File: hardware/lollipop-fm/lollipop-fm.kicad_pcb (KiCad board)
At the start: 2 copper layers, 59 parts, among them J1 battery pads, J2 SWD, J3 USART, Q1 BC817-40W-7, Q2 BC817-40W-7, Q3 SSM3J338R, SW1 MJTP1230F, U1 STM32C011F_4-6_Px, U2 TPS61221DCK, U3 TLV9101IDCKR, U4 TLV9101IDCKR, Y1 ATS08A-E

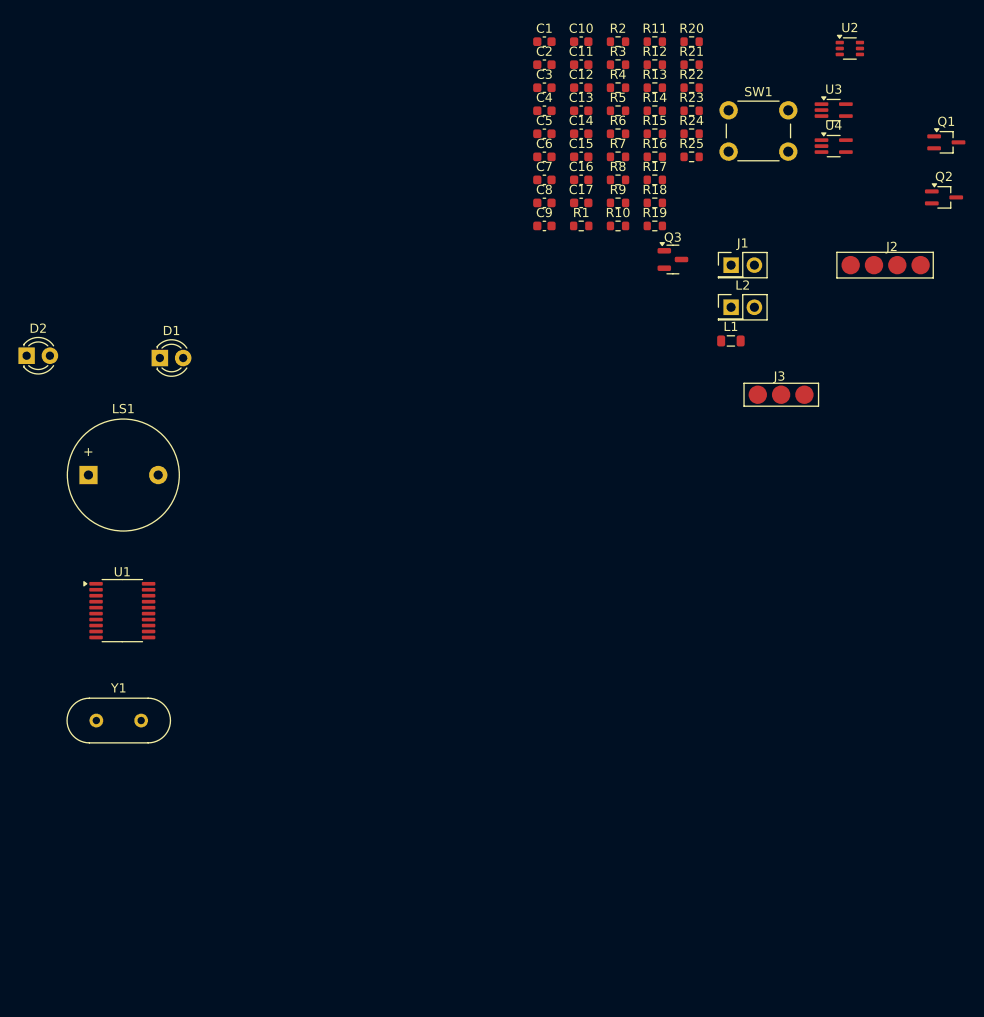
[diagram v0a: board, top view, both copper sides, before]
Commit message: - new routing added
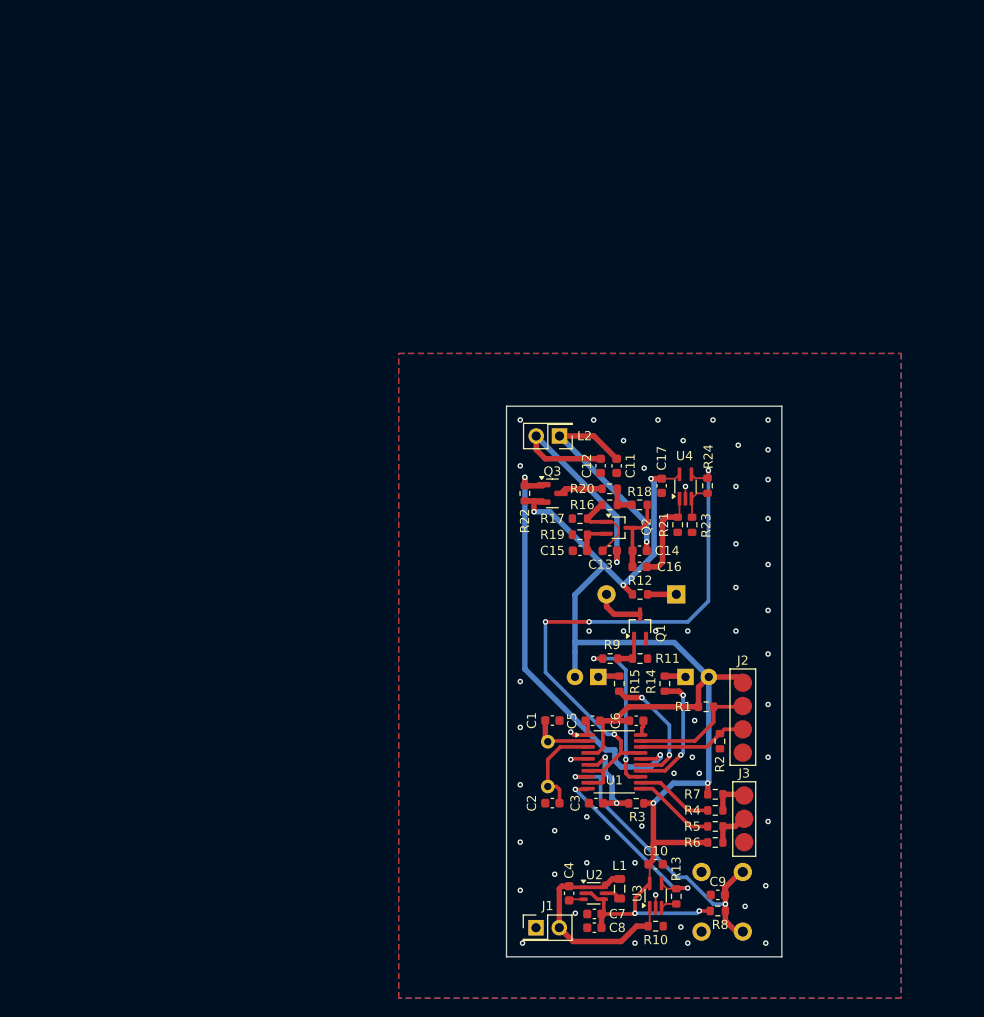
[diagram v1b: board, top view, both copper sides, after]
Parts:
- removed the R8 at (112.2, 75.3)
- D1, D2, LS1, SW1, Y1: moved to B.Cu
- R10: value 100 -> 100k
- moved U2 96.2 mm to (109.5, 153.1)
- moved R13 93.2 mm to (118.5, 153.4), turned to 90 degrees
- moved C10 90.0 mm to (116.2, 149.9)
- moved SW1 89.5 mm to (125.8, 157.2), turned to 90 degrees
- moved U3 87.8 mm to (116.2, 153.3), turned to 90 degrees
- moved C4 85.3 mm to (106.8, 153.1), turned to -90 degrees
- moved R3 80.5 mm to (114.1, 143.3), turned to 180 degrees
- moved C2 80.5 mm to (105.0, 143.2), turned to 180 degrees
- moved C7 80.2 mm to (109.6, 155.3)
- moved R4 79.5 mm to (122.8, 144.0), turned to 180 degrees
- moved C8 79.2 mm to (109.6, 156.8)
- moved R5 78.7 mm to (122.8, 145.8), turned to 180 degrees
- moved C3 78.2 mm to (109.8, 143.2), turned to 180 degrees
- moved R6 77.9 mm to (122.8, 147.5), turned to 180 degrees
- moved R8 77.9 mm to (123.0, 155.0), turned to 180 degrees
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- renumbered R13 to R11, R14 to R12, R11 to R13, R19 to R14, R21 to R15, R15 to R16, R16 to R17, R17 to R18, R18 to R19, R22 to R21, R23 to R22, R24 to R23, R25 to R24, R9 to R8, R12 to R9
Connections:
- R10 pad 1: Net-(R10-Pad1) -> +BATT
- R10 pad 2: /control -> GND
- SW1 pad 1: Net-(R10-Pad1) -> /control
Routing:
- net +3.3V: track 0.00 -> 146.6 mm, vias 0 -> 7
- net /osc_out: track 0.00 -> 63.3 mm, vias 0 -> 4
- net /osc_en: track 0.00 -> 46.8 mm, vias 0 -> 2
- net /control: track 0.00 -> 34.0 mm, vias 0 -> 2
- net Net-(C12-Pad2): track 0.00 -> 27.6 mm, vias 0 -> 1
- net +BATT: track 0.00 -> 24.2 mm
- net Net-(C11-Pad1): track 0.00 -> 23.7 mm, vias 0 -> 1
- net /bat_lvl: track 0.00 -> 21.2 mm, vias 0 -> 2
- net /sound: track 0.00 -> 18.0 mm, vias 0 -> 2
- net /led_yellow: track 0.00 -> 14.0 mm, vias 0 -> 2
- net /led_green: track 0.00 -> 13.9 mm, vias 0 -> 2
- net /SWCLK: track 0.00 -> 13.7 mm
- net /SWDIO: track 0.00 -> 11.9 mm
- net GND: track 0.00 -> 11.6 mm, vias 0 -> 55
- net Net-(U1-PC15): track 0.00 -> 10.8 mm
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- added copper zone on B.Cu, net GND
- added copper zone on F.Cu, net GND
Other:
- board outline added: 30 x 60 mm

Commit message: - production files generated
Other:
- board text added: "+"
- board text added: "-"
- board text added: "F"
- board text added: "LOLLIPOP-FM rev. 1.0"
- board text added: "NON-F"
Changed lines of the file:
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@@
 			(outputformat 1)
 			(mirror no)
-			(drillshape 1)
+			(drillshape 0)
 			(scaleselection 1)
-			(outputdirectory "")
+			(outputdirectory "pcb_1/")
 		)
 	)
@@
 			(at 1.27 -3 0)
 			(layer "B.SilkS")
+			(hide yes)
 			(effects
 				(font
@@
 			(at 1.21 -3.25 0)
 			(layer "B.SilkS")
+			(hide yes)
 			(effects
 				(font
@@
 		(layer "Edge.Cuts")
 	)
+	(gr_text "F"
+		(at 109 133.25 0)
+		(layer "B.SilkS")
+		(effects
+			(font
+				(size 1 1)
+				(thickness 0.25)
+				(bold yes)
+			)
+			(justify left bottom mirror)
+		)
+	)
+	(gr_text "NON-F"
+		(at 123.25 133.25 0)
+		(layer "B.SilkS")
+		(effects
+			(font
+				(size 1 1)
+				(thickness 0.25)
+				(bold yes)
+			)
+			(justify left bottom mirror)
+		)
+	)
+	(gr_text "+"
+		(at 107.5 155 0)
+		(layer "B.SilkS")
+		(effects
+			(font
+				(size 2 2)
+				(thickness 0.5)
+				(bold yes)
+			)
+			(justify left bottom mirror)
+		)
+	)
+	(gr_text "LOLLIPOP-FM rev. 1.0"
+		(at 125.75 125.75 270)
+		(layer "B.SilkS")
+		(effects
+			(font
+				(size 1 1)
+				(thickness 0.25)
+				(bold yes)
+			)
+			(justify left bottom mirror)
+		)
+	)
+	(gr_text "-"
+		(at 104.5 155 0)
+		(layer "B.SilkS")
+		(effects
+			(font
+				(size 2 2)
+				(thickness 0.5)
+				(bold yes)
+			)
+			(justify left bottom mirror)
+		)
+	)
 	(segment

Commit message: - led control logic updated, schematic naming updated
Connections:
- net /led_green renamed /led_non_f
- net /led_yellow renamed /led_f
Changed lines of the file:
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@@
 	(net 30 "/sound")
 	(net 31 "Net-(R16-Pad1)")
-	(net 32 "/led_green")
-	(net 33 "/led_yellow")
+	(net 32 "/led_non_f")
+	(net 33 "/led_f")
 	(net 34 "Net-(U4--)")
 	(net 35 "/osc_out")
@@
 			(layers "F.Cu" "F.Mask" "F.Paste")
 			(roundrect_rratio 0.25)
-			(net 32 "/led_green")
+			(net 32 "/led_non_f")
 			(pinfunction "PA7")
 			(pintype "bidirectional")
@@
 			(layers "F.Cu" "F.Mask" "F.Paste")
 			(roundrect_rratio 0.25)
-			(net 33 "/led_yellow")
+			(net 33 "/led_f")
 			(pinfunction "PA8")
 			(pintype "bidirectional")
@@
 			(layers "F.Cu" "F.Mask" "F.Paste")
 			(roundrect_rratio 0.25)
-			(net 32 "/led_green")
+			(net 32 "/led_non_f")
 			(pintype "passive")
 		)
@@
 			(layers "F.Cu" "F.Mask" "F.Paste")
 			(roundrect_rratio 0.25)
-			(net 33 "/led_yellow")
+			(net 33 "/led_f")
 			(pintype "passive")
 		)
